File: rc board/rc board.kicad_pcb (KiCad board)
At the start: 2 copper layers, 54 parts, among them J1 Bypass, J10 3S, J11 4S, J12 5S, J13 6S, J14 Mot_0, J15 Mot_0, J2 Bypass, J3 Bypass, J4 Throttle_in, J5 Throttle_out, J6 CH3_in, J7 CH3_out, J8 Steering_in, J9 Steering_out, U1 DRV10983, U2 DRV10983

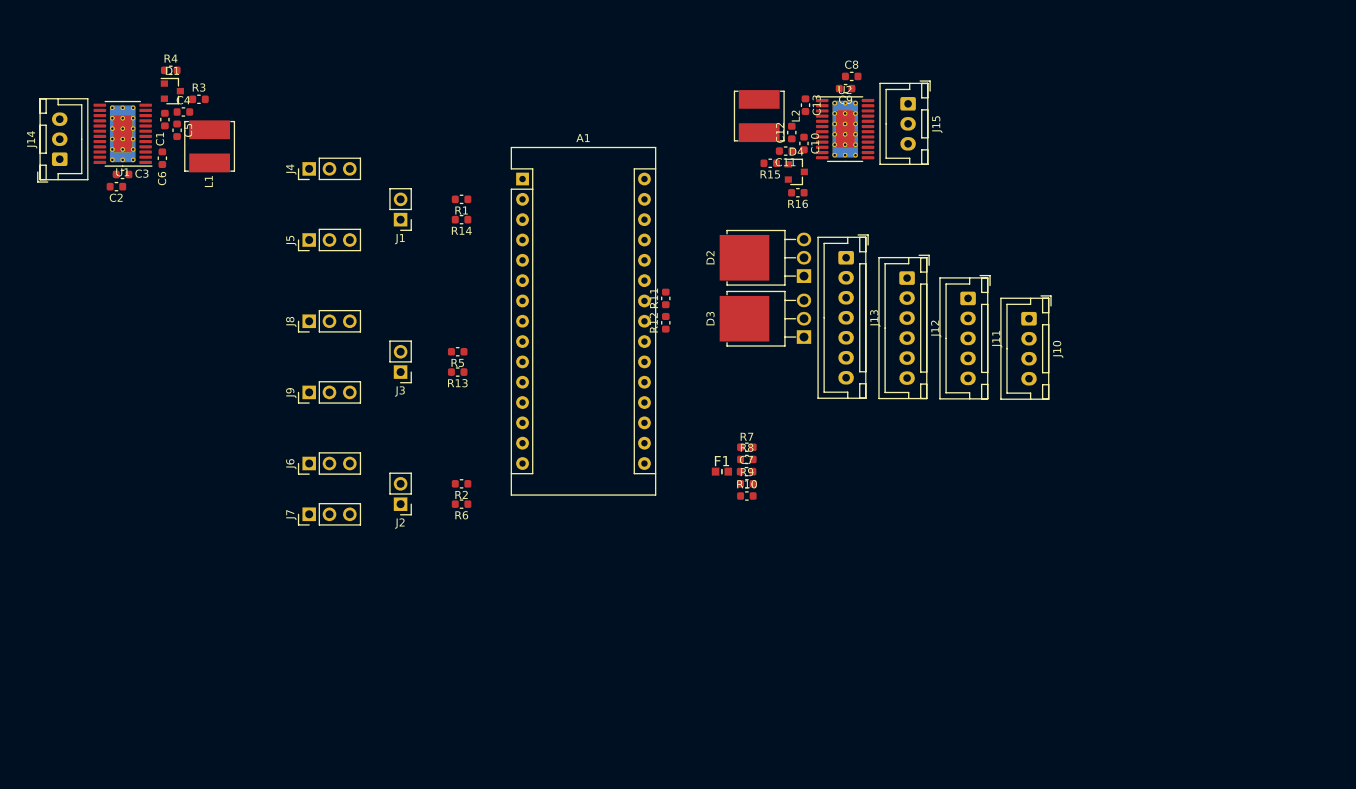
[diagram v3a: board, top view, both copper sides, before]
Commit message: Added and placed the last 2 drivers, added the battery monitoring part.
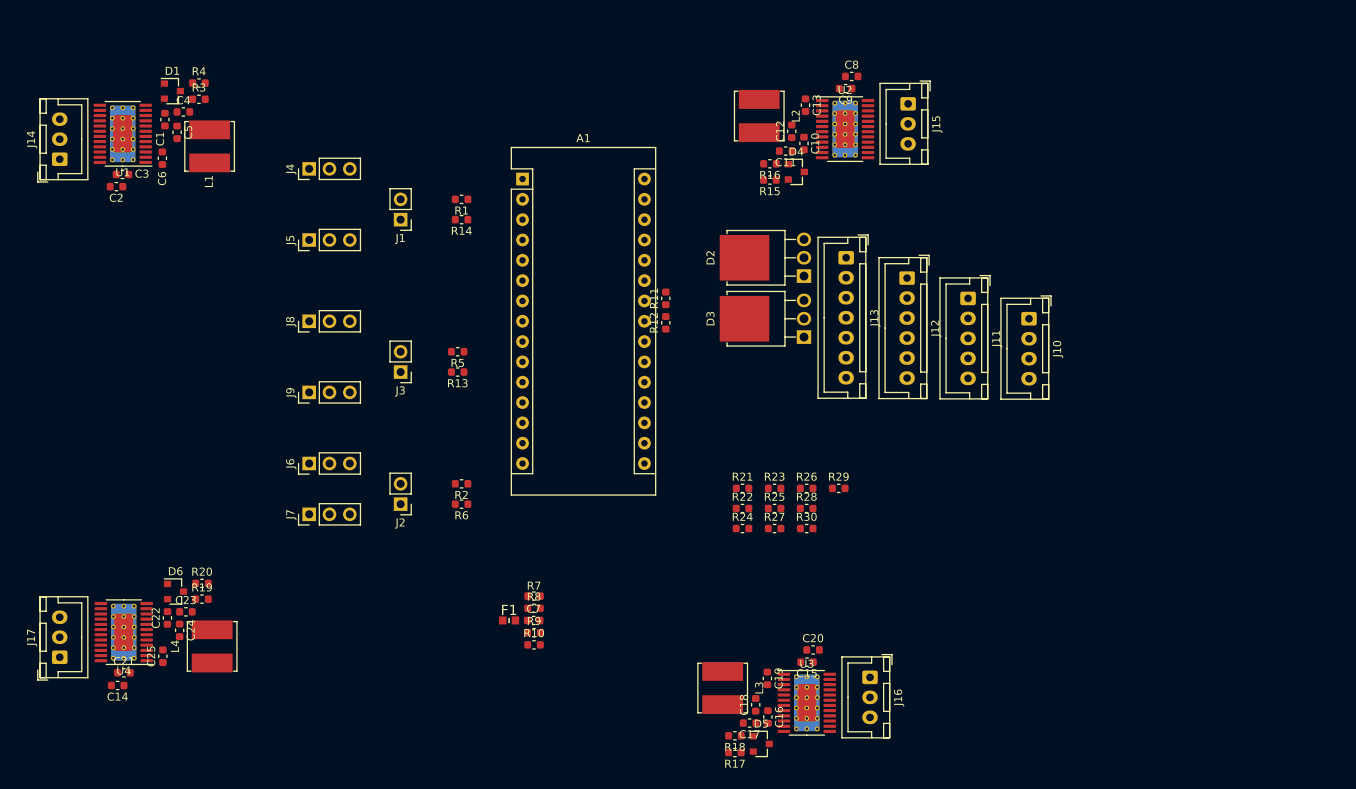
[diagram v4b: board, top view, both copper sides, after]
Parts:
- added C14: 10uF, Capacitor_SMD:C_0603_1608Metric, F.Cu at (25.8, 92.1)
- added C15: 100nF, Capacitor_SMD:C_0603_1608Metric, F.Cu at (112.0, 89.2)
- added C16: 1uF, Capacitor_SMD:C_0603_1608Metric, F.Cu at (107.1, 96.1)
- added C17: 10uF, Capacitor_SMD:C_0603_1608Metric, F.Cu at (104.8, 96.8)
- added C18: 1uF, Capacitor_SMD:C_0603_1608Metric, F.Cu at (105.6, 94.6)
- added C19: 10nF, Capacitor_SMD:C_0603_1608Metric, F.Cu at (107.1, 91.2)
- added C20: 10uF, Capacitor_SMD:C_0603_1608Metric, F.Cu at (112.8, 87.7)
- added C21: 100nF, Capacitor_SMD:C_0603_1608Metric, F.Cu at (26.6, 90.6)
- added C22: 1uF, Capacitor_SMD:C_0603_1608Metric, F.Cu at (32.1, 83.7)
- added C23: 10uF, Capacitor_SMD:C_0603_1608Metric, F.Cu at (34.4, 82.9)
- added C24: 1uF, Capacitor_SMD:C_0603_1608Metric, F.Cu at (33.6, 85.2)
- added C25: 10nF, Capacitor_SMD:C_0603_1608Metric, F.Cu at (31.5, 88.5)
- added D5: BAW56LT3G, Package_TO_SOT_SMD:SOT-23, F.Cu at (106.3, 99.4)
- added D6: BAW56LT3G, Package_TO_SOT_SMD:SOT-23, F.Cu at (33.1, 80.4)
- added J16: Mot_0, Connector_JST:JST_XH_B3B-XH-A_1x03_P2.50mm_Vertical, F.Cu at (119.9, 91.1)
- added J17: Mot_0, Connector_JST:JST_XH_B3B-XH-A_1x03_P2.50mm_Vertical, F.Cu at (18.6, 88.6)
- added L3: 47 uH, Inductor_SMD:L_Bourns_SRN6045TA, F.Cu at (101.5, 92.5)
- added L4: 47 uH, Inductor_SMD:L_Bourns_SRN6045TA, F.Cu at (37.7, 87.2)
- added R17: 10k, Resistor_SMD:R_0603_1608Metric, F.Cu at (103.0, 100.5)
- added R18: 10k, Resistor_SMD:R_0603_1608Metric, F.Cu at (103.0, 98.4)
- added R19: 10k, Resistor_SMD:R_0603_1608Metric, F.Cu at (36.4, 81.3)
- added R20: 10k, Resistor_SMD:R_0603_1608Metric, F.Cu at (36.4, 79.4)
- added R21: 100k, Resistor_SMD:R_0603_1608Metric, F.Cu at (103.9, 67.5)
- added R22: 150k, Resistor_SMD:R_0603_1608Metric, F.Cu at (103.9, 70.0)
- added R23: 180k, Resistor_SMD:R_0603_1608Metric, F.Cu at (108.0, 67.5)
- added R24: 330k, Resistor_SMD:R_0603_1608Metric, F.Cu at (103.9, 72.5)
- added R25: 470k, Resistor_SMD:R_0603_1608Metric, F.Cu at (108.0, 70.0)
- added R26: 560k, Resistor_SMD:R_0603_1608Metric, F.Cu at (112.0, 67.5)
- added R27: 560k, Resistor_SMD:R_0603_1608Metric, F.Cu at (108.0, 72.5)
- added R28: 560k, Resistor_SMD:R_0603_1608Metric, F.Cu at (112.0, 70.0)
- added R29: 560k, Resistor_SMD:R_0603_1608Metric, F.Cu at (116.0, 67.5)
- added R30: 560k, Resistor_SMD:R_0603_1608Metric, F.Cu at (112.0, 72.5)
- added U3: DRV10983, Package_SO:HTSSOP-24-1EP_4.4x7.8mm_P0.65mm_EP3.4x7.8mm_Mask2.4x4.68mm_ThermalVias, F.Cu at (112.0, 94.3)
- added U4: DRV10983, Package_SO:HTSSOP-24-1EP_4.4x7.8mm_P0.65mm_EP3.4x7.8mm_Mask2.4x4.68mm_ThermalVias, F.Cu at (26.6, 85.5)
- moved R7 32.5 mm to (77.9, 81.0)
- moved R8 32.5 mm to (77.9, 82.5)
- moved R10 32.5 mm to (77.9, 87.1)
- moved R9 32.5 mm to (77.9, 85.5)
- moved C7 32.5 mm to (77.9, 84.0)
- moved F1 32.5 mm to (74.8, 84.0)
- moved R16 5.03 mm to (107.4, 26.9)
- moved R4 3.86 mm to (36.0, 16.8)
- moved R15 2.10 mm to (107.4, 29.0)
- moved C5 0.25 mm to (33.3, 23.0)
- moved C12 0.16 mm to (110.1, 22.9)
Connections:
- A1 pad 19: Batt_0_sense -> Batt_0
- R13 pad 1: Net-(A1-Pad15) -> Net-(A1-Pad13)
- R2 pad 1: Net-(A1-Pad8) -> Net-(A1-Pad12)
- R5 pad 1: Net-(A1-Pad12) -> Net-(A1-Pad8)
- R6 pad 1: Net-(A1-Pad13) -> Net-(A1-Pad15)

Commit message: Placed the battery monitoring system.
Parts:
- moved R26 34.7 mm to (96.8, 36.3), turned to 180 degrees
- moved R27 32.6 mm to (96.8, 41.8), turned to 180 degrees
- moved R22 30.5 mm to (96.8, 40.3)
- moved R21 30.5 mm to (96.8, 37.8)
- moved R28 28.1 mm to (96.8, 46.4), turned to 180 degrees
- moved R29 25.5 mm to (96.8, 50.8), turned to 180 degrees
- moved R23 25.3 mm to (96.8, 44.8)
- moved R24 24.3 mm to (96.8, 49.3)
- moved R30 23.8 mm to (96.8, 54.2), turned to 180 degrees
- moved R25 20.6 mm to (96.8, 52.7)
- moved C16 9.69 mm to (112.2, 87.8)
- moved C17 9.69 mm to (109.9, 88.6)
- moved C18 9.69 mm to (110.7, 86.3)
- moved L3 9.69 mm to (106.6, 84.2)
- moved C15 9.69 mm to (117.1, 81.0)
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
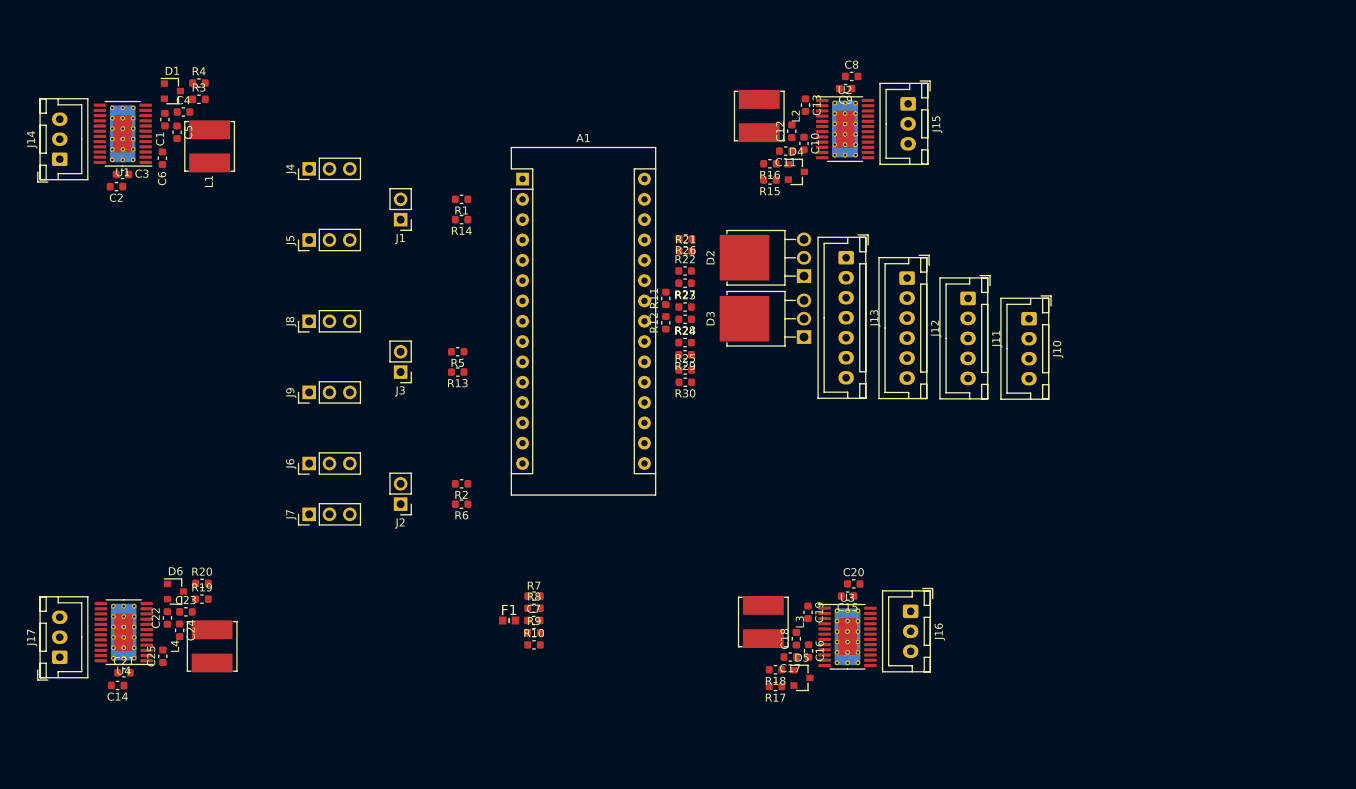
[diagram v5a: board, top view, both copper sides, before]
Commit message: Layed down almost all the components but the capacitors.
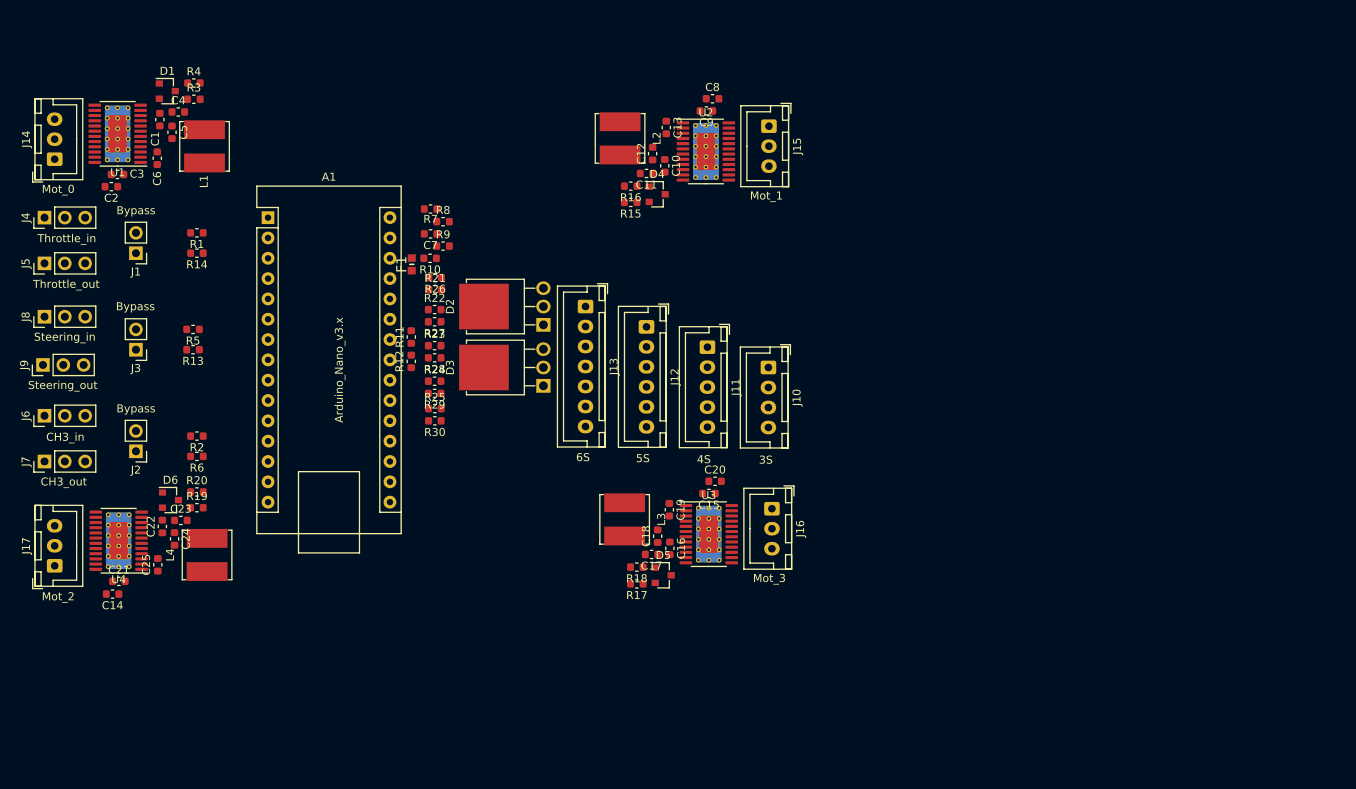
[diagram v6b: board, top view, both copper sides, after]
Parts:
- J15: value Mot_0 -> Mot_1
- J16: value Mot_0 -> Mot_3
- J17: value Mot_0 -> Mot_2
- moved R7 50.1 mm to (65.0, 32.6), turned to 180 degrees
- moved R10 50.0 mm to (64.9, 38.7), turned to 180 degrees
- moved C7 50.0 mm to (65.0, 35.7), turned to 180 degrees
- moved R8 49.6 mm to (66.5, 34.2)
- moved R9 49.6 mm to (66.5, 37.2)
- moved F1 46.1 mm to (62.6, 39.5), turned to 90 degrees
- moved J2 33.7 mm to (28.1, 62.9)
- moved J7 33.7 mm to (16.7, 64.1)
- moved J4 33.6 mm to (16.7, 33.7)
- moved R2 33.6 mm to (35.8, 61.0)
- moved J6 33.6 mm to (16.7, 58.4)
- moved R6 33.6 mm to (35.8, 63.5)
- moved J9 33.5 mm to (16.5, 52.1)
- moved J1 33.3 mm to (28.1, 38.1)
- moved R1 33.3 mm to (35.8, 35.6)
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
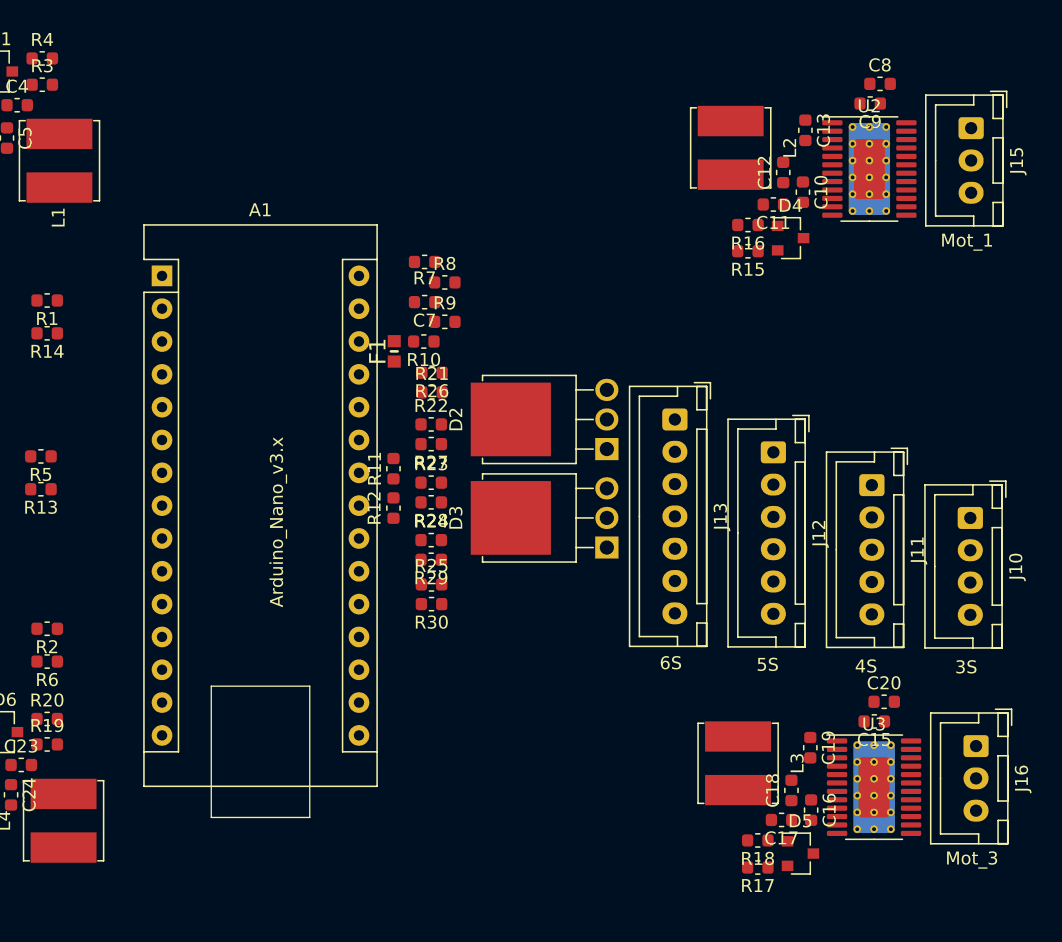
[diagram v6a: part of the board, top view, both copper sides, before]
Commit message: Added caps (everybody loves caps), and placed all the components.
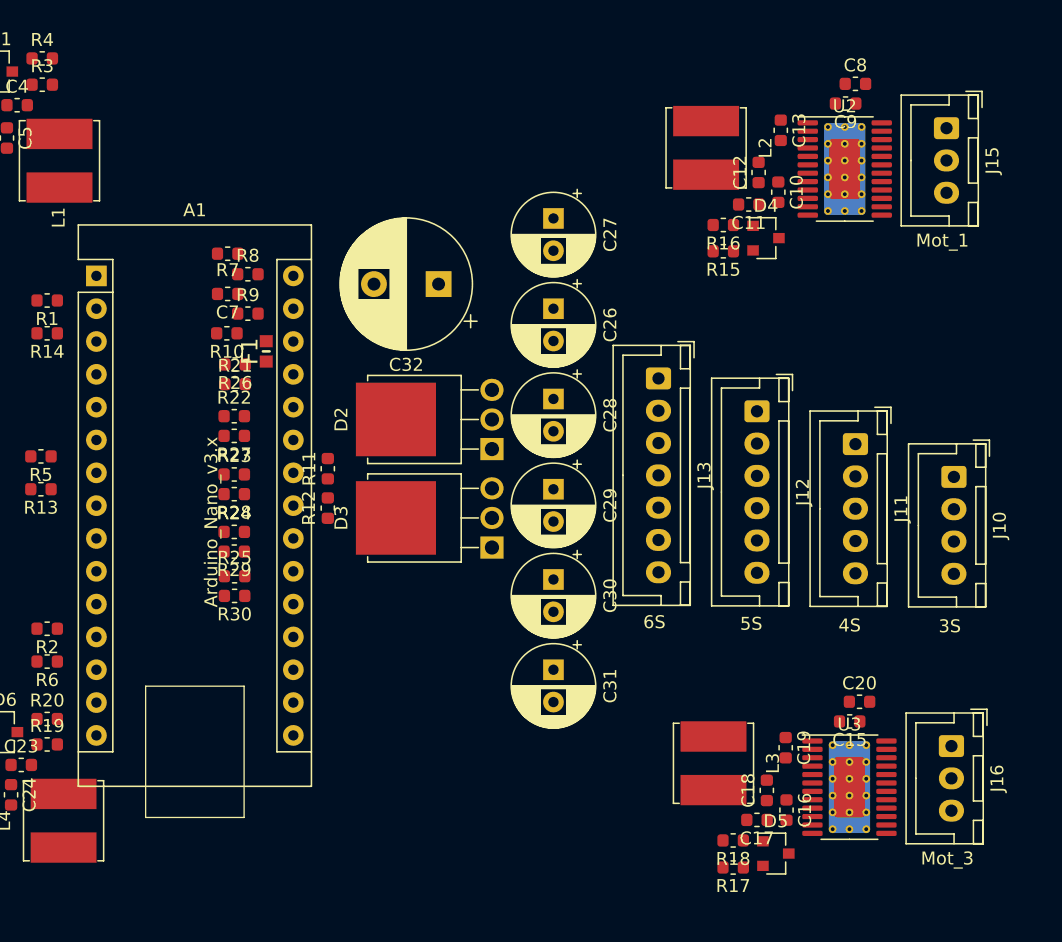
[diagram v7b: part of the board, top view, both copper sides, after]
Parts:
- added C26: 1000uF, Capacitor_THT:CP_Radial_D6.3mm_P2.50mm, F.Cu at (74.9, 36.2)
- added C27: 1000uF, Capacitor_THT:CP_Radial_D6.3mm_P2.50mm, F.Cu at (74.9, 29.2)
- added C28: 1000uF, Capacitor_THT:CP_Radial_D6.3mm_P2.50mm, F.Cu at (74.9, 43.2)
- added C29: 1000uF, Capacitor_THT:CP_Radial_D6.3mm_P2.50mm, F.Cu at (74.9, 50.2)
- added C30: 1000uF, Capacitor_THT:CP_Radial_D6.3mm_P2.50mm, F.Cu at (74.9, 57.1)
- added C31: 1000uF, Capacitor_THT:CP_Radial_D6.3mm_P2.50mm, F.Cu at (74.9, 64.1)
- added C32: 1000uF, Capacitor_THT:CP_Radial_D10.0mm_P5.00mm, F.Cu at (66.0, 34.3)
- moved R10 15.3 mm to (49.7, 38.1)
- moved R22 15.3 mm to (50.2, 44.5)
- moved R23 15.3 mm to (50.2, 49.0)
- moved R24 15.3 mm to (50.2, 53.5)
- moved R27 15.3 mm to (50.2, 46.0)
- moved R28 15.3 mm to (50.2, 50.5)
- moved R29 15.3 mm to (50.2, 55.0)
- moved R25 15.3 mm to (50.3, 56.9)
- moved R30 15.3 mm to (50.3, 58.4)
- moved C7 15.3 mm to (49.7, 35.1)
- moved R21 15.3 mm to (50.3, 42.0)
- moved R26 15.3 mm to (50.3, 40.5)
- moved R7 15.3 mm to (49.7, 31.9)
- moved R8 15.3 mm to (51.3, 33.5)
- moved R9 15.3 mm to (51.3, 36.6)
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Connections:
- D2 pad 3: Batt_5 -> Net-(C26-Pad2)
- J10 pad 1: Batt_2 -> Net-(C28-Pad2)
- J10 pad 2: Batt_1 -> Net-(C29-Pad2)
- J10 pad 3: Batt_0 -> Net-(C30-Pad2)
- J11 pad 1: Batt_3 -> Net-(C27-Pad2)
- J11 pad 2: Batt_2 -> Net-(C28-Pad2)
- J11 pad 3: Batt_1 -> Net-(C29-Pad2)
- J11 pad 4: Batt_0 -> Net-(C30-Pad2)
- J12 pad 1: Batt_4 -> Net-(C26-Pad1)
- J12 pad 2: Batt_3 -> Net-(C27-Pad2)
- J12 pad 3: Batt_2 -> Net-(C28-Pad2)
- J12 pad 4: Batt_1 -> Net-(C29-Pad2)
- J12 pad 5: Batt_0 -> Net-(C30-Pad2)
- J13 pad 1: Batt_5 -> Net-(C26-Pad2)
- J13 pad 2: Batt_4 -> Net-(C26-Pad1)
- J13 pad 3: Batt_3 -> Net-(C27-Pad2)
- J13 pad 4: Batt_2 -> Net-(C28-Pad2)
- J13 pad 5: Batt_1 -> Net-(C29-Pad2)
- J13 pad 6: Batt_0 -> Net-(C30-Pad2)
